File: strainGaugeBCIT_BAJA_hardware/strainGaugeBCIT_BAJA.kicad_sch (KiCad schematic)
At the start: 2 parts, among them U2 AD620

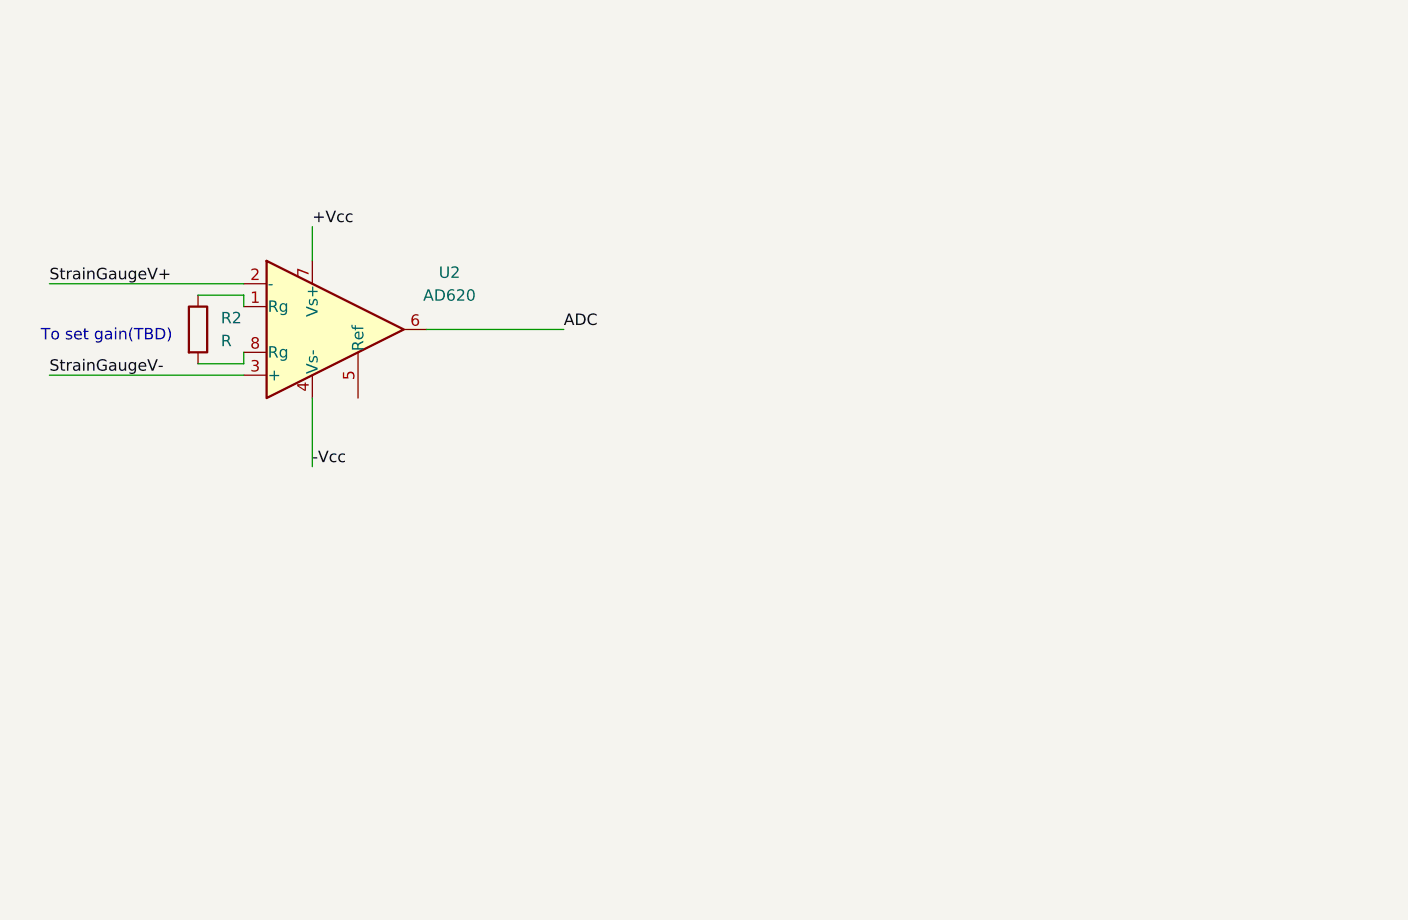
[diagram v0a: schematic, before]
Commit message: adding stm32 attempt 2
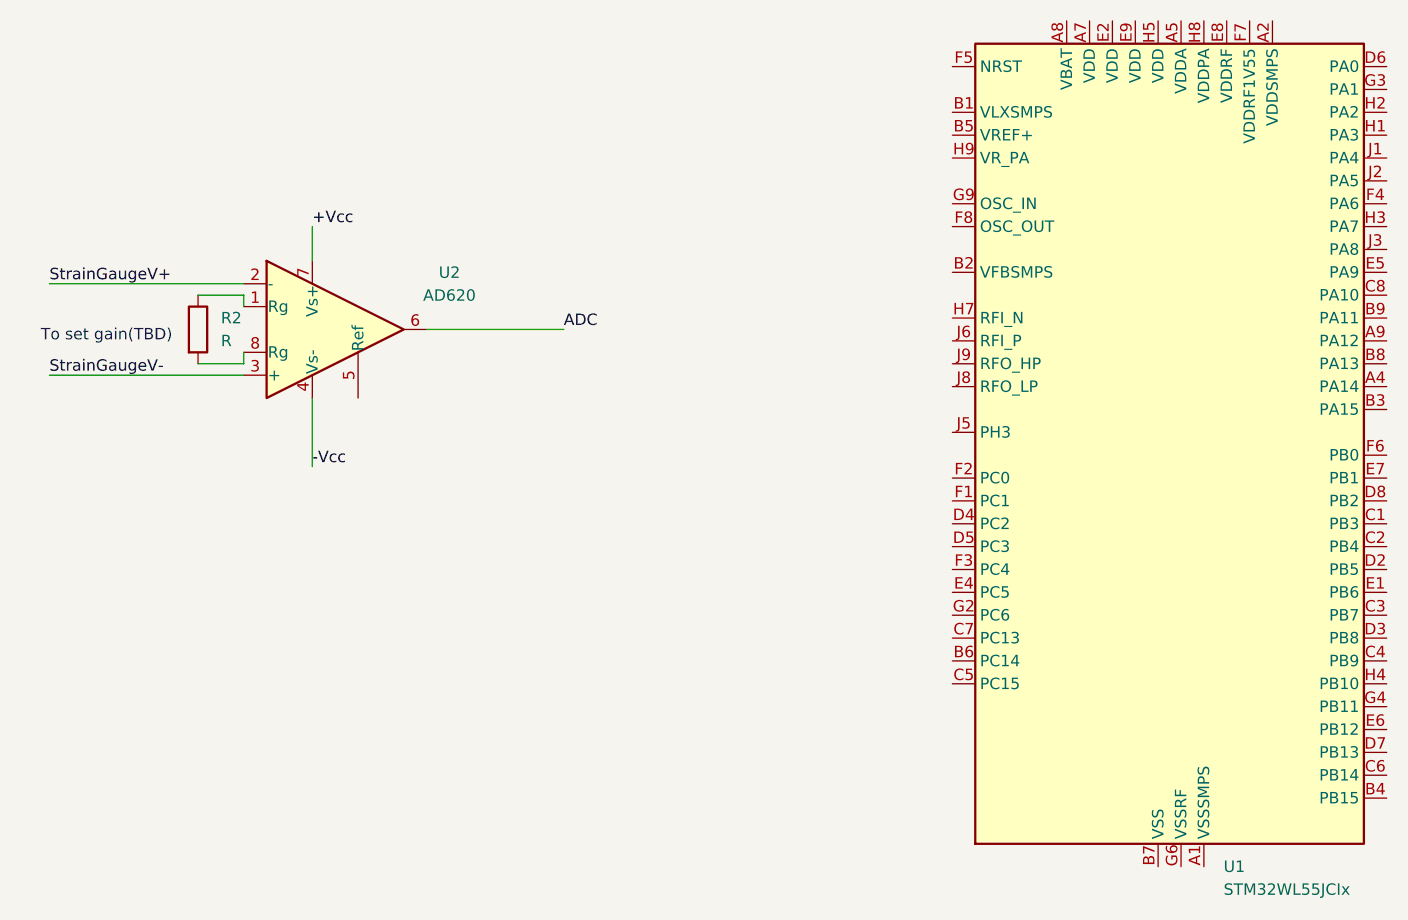
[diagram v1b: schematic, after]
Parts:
- added U1: STM32WL55JCIx, Package_BGA:ST_UFBGA-73_5x5mm_Layout9x9_P0.5mm, symbol MCU_ST_STM32WL:STM32WL55JCIx
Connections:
- new net: U1.B7 (VSS), U1.D9 (VSS), U1.E3 (VSS), U1.G5 (VSS)
- new net: U1.G6 (VSSRF), U1.G7 (VSSRF), U1.G8 (VSSRF), U1.H6 (VSSRF)
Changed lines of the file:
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@@
+	)
+	(symbol
+		(lib_id "MCU_ST_STM32WL:STM32WL55JCIx")
+		(at 153.67 91.44 0)
+		(unit 1)
+		(exclude_from_sim no)
+		(in_bom yes)
+		(on_board yes)
+		(dnp no)
+		(fields_autoplaced yes)
+		(property "Reference" "U1"
+			(at 160.9441 137.16 0)
+			(effects
+				(font
+					(size 1.27 1.27)
+				)
+				(justify left)
+			)
+		)
+		(property "Value" "STM32WL55JCIx"
+			(at 160.9441 139.7 0)
+			(effects
+				(font
+					(size 1.27 1.27)
+				)
+				(justify left)
+			)
+		)
+		(property "Footprint" "Package_BGA:ST_UFBGA-73_5x5mm_Layout9x9_P0.5mm"
+			(at 133.35 134.62 0)
+			(effects
+				(font
+					(size 1.27 1.27)
+				)
+				(justify right)
+				(hide yes)
+			)
+		)
+		(property "Datasheet" "https://www.st.com/resource/en/datasheet/stm32wl55jc.pdf"
+			(at 153.67 91.44 0)
+			(effects
+				(font
+					(size 1.27 1.27)
+				)
+				(hide yes)
+			)
+		)
+		(property "Description" "STMicroelectronics Arm Cortex-M4 MCU, 256KB flash, 64KB RAM, 48 MHz, 1.8-3.6V, 43 GPIO, UFBGA73"
+			(at 153.67 91.44 0)
+			(effects
+				(font
+					(size 1.27 1.27)
+				)
+				(hide yes)
+			)
+		)
+		(pin "C8"
+		)
+		(pin "A1"
+		)
+		(pin "A8"
+		)
+		(pin "D9"
+		)
+		(pin "E9"
+		)
+		(pin "E4"
+		)
+		(pin "A9"
+		)
+		(pin "C5"
+		)
+		(pin "B9"
+		)
+		(pin "D3"
+		)
+		(pin "D4"
+		)
+		(pin "E1"
+		)
+		(pin "G5"
+		)
+		(pin "C1"
+		)
+		(pin "C4"
+		)
+		(pin "B7"
+		)
+		(pin "E8"
+		)
+		(pin "C3"
+		)
+		(pin "A4"
+		)
+		(pin "D8"
+		)
+		(pin "F3"
+		)
+		(pin "G6"
+		)
+		(pin "B6"
+		)
+		(pin "B8"
+		)
+		(pin "B3"
+		)
+		(pin "A5"
+		)
+		(pin "B1"
+		)
+		(pin "A2"
+		)
+		(pin "C7"
+		)
+		(pin "D6"
+		)
+		(pin "A7"
+		)
+		(pin "B2"
+		)
+		(pin "C2"
+		)
+		(pin "C6"
+		)
+		(pin "D7"
+		)
+		(pin "F4"
+		)
+		(pin "D2"
+		)
+		(pin "B5"
+		)
+		(pin "E3"
+		)
+		(pin "E5"
+		)
+		(pin "E6"
+		)
+		(pin "B4"
+		)
+		(pin "D5"
+		)
+		(pin "E2"
+		)
+		(pin "E7"
+		)
+		(pin "F1"
+		)
+		(pin "F2"
+		)
+		(pin "F5"
+		)
+		(pin "F6"
+		)
+		(pin "F7"
+		)
+		(pin "F8"
+		)
+		(pin "G2"
+		)
+		(pin "G3"
+		)
+		(pin "G4"
+		)
+		(pin "G7"
+		)
+		(pin "G8"
+		)
+		(pin "H7"
+		)
+		(pin "H2"
+		)
+		(pin "H9"
+		)
+		(pin "J3"
+		)
+		(pin "J6"
+		)
+		(pin "J5"
+		)
+		(pin "H5"
+		)
+		(pin "J9"
+		)
+		(pin "J1"
+		)
+		(pin "H3"
+		)
+		(pin "G9"
+		)
+		(pin "H4"
+		)
+		(pin "H8"
+		)
+		(pin "J2"
+		)
+		(pin "J8"
+		)
+		(pin "H1"
+		)
+		(pin "H6"
+		)
+		(instances
+			(project "strainGaugeBCIT_BAJA"
+				(path "/8162a86f-8c2b-4bf1-82ac-a8a91f9f1fb6"
+					(reference "U1")
+					(unit 1)
+				)
+			)
+		)
 	)
 	(symbol
